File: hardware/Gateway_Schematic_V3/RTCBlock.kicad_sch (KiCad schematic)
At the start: 6 parts, among them IC1 RTC_DS3231M

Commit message: Update PCB Layout for Gateway (24/3/2026)
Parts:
- added GND0: TestPoint, IVS_NEW_FOOTPRINT:TestPoint_throughtHole_D1.0mm, symbol Connector:TestPoint
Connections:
- net GND: now also GND0.1
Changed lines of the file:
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@@
+	)
+	(junction
+		(at 142.24 107.95)
+		(diameter 0)
+		(color 0 0 0 0)
 	)
 	(junction
@@
 	(wire
 		(pts
+			(xy 142.24 107.95) (xy 142.24 104.14)
+		)
+		(stroke
+			(width 0)
+			(type default)
+		)
+	)
+	(wire
+		(pts
 			(xy 124.46 72.39) (xy 124.46 77.47)
 		)
@@
 	(wire
 		(pts
-			(xy 142.24 106.68) (xy 142.24 104.14)
+			(xy 142.24 113.03) (xy 142.24 107.95)
 		)
 		(stroke
@@
 		)
 	)
+	(wire
+		(pts
+			(xy 133.35 110.49) (xy 133.35 107.95)
+		)
+		(stroke
+			(width 0)
+			(type default)
+		)
+	)
 	(bus
 		(pts
 			(xy 114.3 88.9) (xy 114.3 91.44)
+		)
+		(stroke
+			(width 0)
+			(type default)
+		)
+	)
+	(wire
+		(pts
+			(xy 133.35 107.95) (xy 142.24 107.95)
 		)
 		(stroke
@@
 			)
 			(justify right)
+		)
+	)
+	(symbol
+		(lib_id "Connector:TestPoint")
+		(at 133.35 110.49 180)
+		(unit 1)
+		(exclude_from_sim no)
+		(in_bom yes)
+		(on_board yes)
+		(dnp no)
+		(property "Reference" "GND0"
+			(at 132.08 116.078 0)
+			(effects
+				(font
+					(size 1.27 1.27)
+				)
+				(justify right)
+			)
+		)
+		(property "Value" "TestPoint"
+			(at 135.89 115.0619 0)
+			(effects
+				(font
+					(size 1.27 1.27)
+				)
+				(justify right)
+				(hide yes)
+			)
+		)
+		(property "Footprint" "IVS_NEW_FOOTPRINT:TestPoint_throughtHole_D1.0mm"
+			(at 128.27 110.49 0)
+			(effects
+				(font
+					(size 1.27 1.27)
+				)
+				(hide yes)
+			)
+		)
+		(property "Datasheet" "~"
+			(at 128.27 110.49 0)
+			(effects
+				(font
+					(size 1.27 1.27)
+				)
+				(hide yes)
+			)
+		)
+		(property "Description" "test point"
+			(at 133.35 110.49 0)
+			(effects
+				(font
+					(size 1.27 1.27)
+				)
+				(hide yes)
+			)
+		)
+		(pin "1"
+		)
+		(instances
+			(project "Schematic_V2_backup"
+				(path "/08b065f5-231d-43cb-bb9e-87dca43beac9/b64c8f51-171e-4949-97e6-87303bf3a90b"
+					(reference "GND0")
+					(unit 1)
+				)
+			)
 		)
 	)
@@
 	(symbol
 		(lib_id "power:GND")
-		(at 142.24 106.68 0)
+		(at 142.24 113.03 0)
 		(unit 1)
 		(exclude_from_sim no)
@@
 		(fields_autoplaced yes)
 		(property "Reference" "#PWR06"
+			(at 142.24 119.38 0)
+			(effects
+				(font
+					(size 1.27 1.27)
+				)
+				(hide yes)
+			)
+		)
+		(property "Value" "GND"
+			(at 144.78 114.2999 0)
+			(effects
+				(font
+					(size 1.27 1.27)
+				)
+				(justify left)
+			)
+		)
+		(property "Footprint" ""
 			(at 142.24 113.03 0)
 			(effects
@@
 			)
 		)
-		(property "Value" "GND"
-			(at 144.78 107.9499 0)
-			(effects
-				(font
-					(size 1.27 1.27)
-				)
-				(justify left)
-			)
-		)
-		(property "Footprint" ""
-			(at 142.24 106.68 0)
-			(effects
-				(font
-					(size 1.27 1.27)
-				)
-				(hide yes)
-			)
-		)
 		(property "Datasheet" ""
-			(at 142.24 106.68 0)
+			(at 142.24 113.03 0)
 			(effects
 				(font
@@
 		)
 		(property "Description" "Power symbol creates a global label with name \"GND\" , ground"
-			(at 142.24 106.68 0)
-			(effects
-				(font
+			(at 142.24 113.03 0)
+			(effects
+				(font

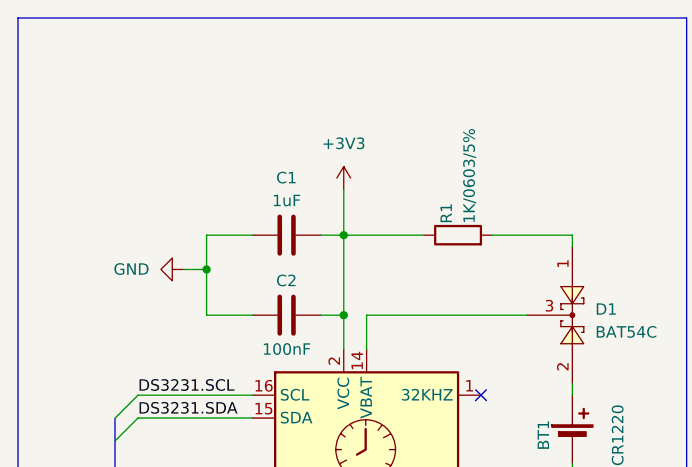
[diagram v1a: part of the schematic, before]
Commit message: Update PCB Layout after review 27/3/2026
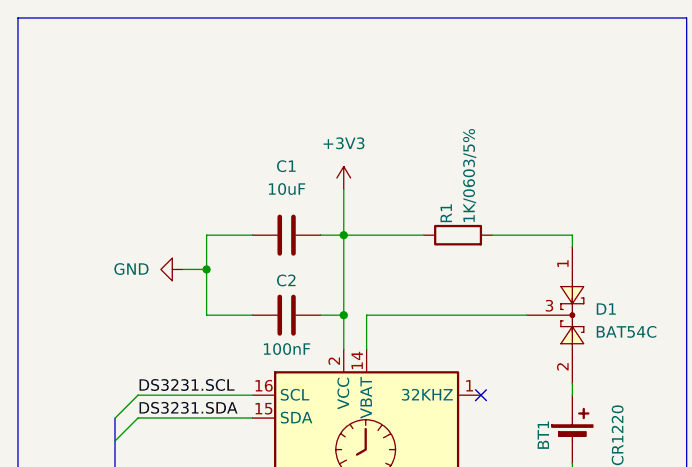
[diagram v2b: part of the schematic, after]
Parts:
- C1: value 1uF -> 10uF
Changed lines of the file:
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@@
 		(fields_autoplaced yes)
 		(property "Reference" "C1"
-			(at 133.35 62.23 90)
+			(at 133.35 60.96 90)
 			(effects
 				(font
@@
 			)
 		)
-		(property "Value" "1uF"
-			(at 133.35 64.77 90)
+		(property "Value" "10uF"
+			(at 133.35 63.5 90)
 			(effects
 				(font
